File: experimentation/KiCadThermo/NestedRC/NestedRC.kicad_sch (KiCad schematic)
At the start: 12 parts

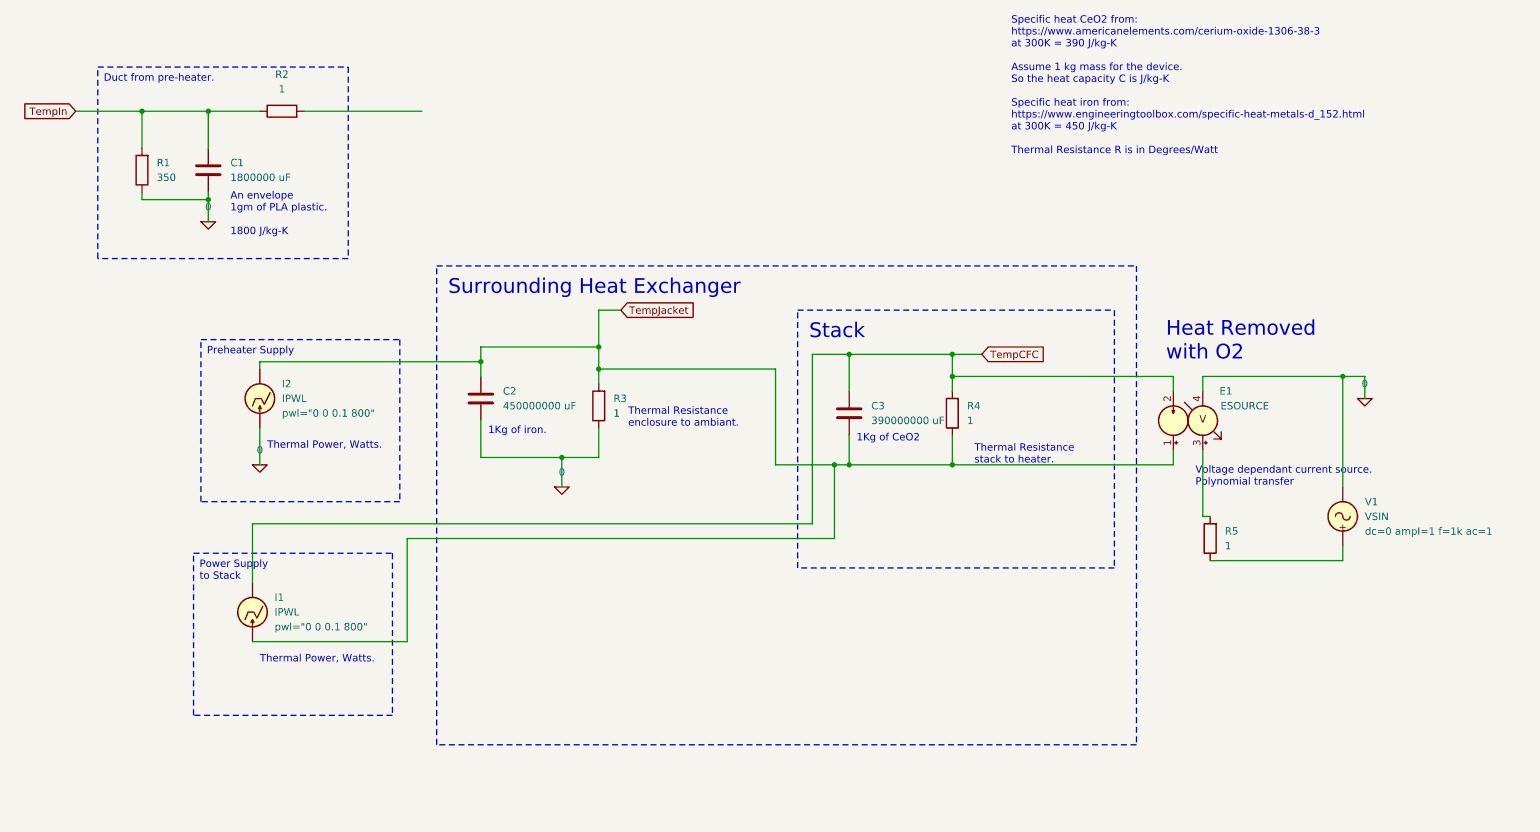
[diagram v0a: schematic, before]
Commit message: Add GPOLY to NestedRC circuit and set some values to make plots with which to experiment.
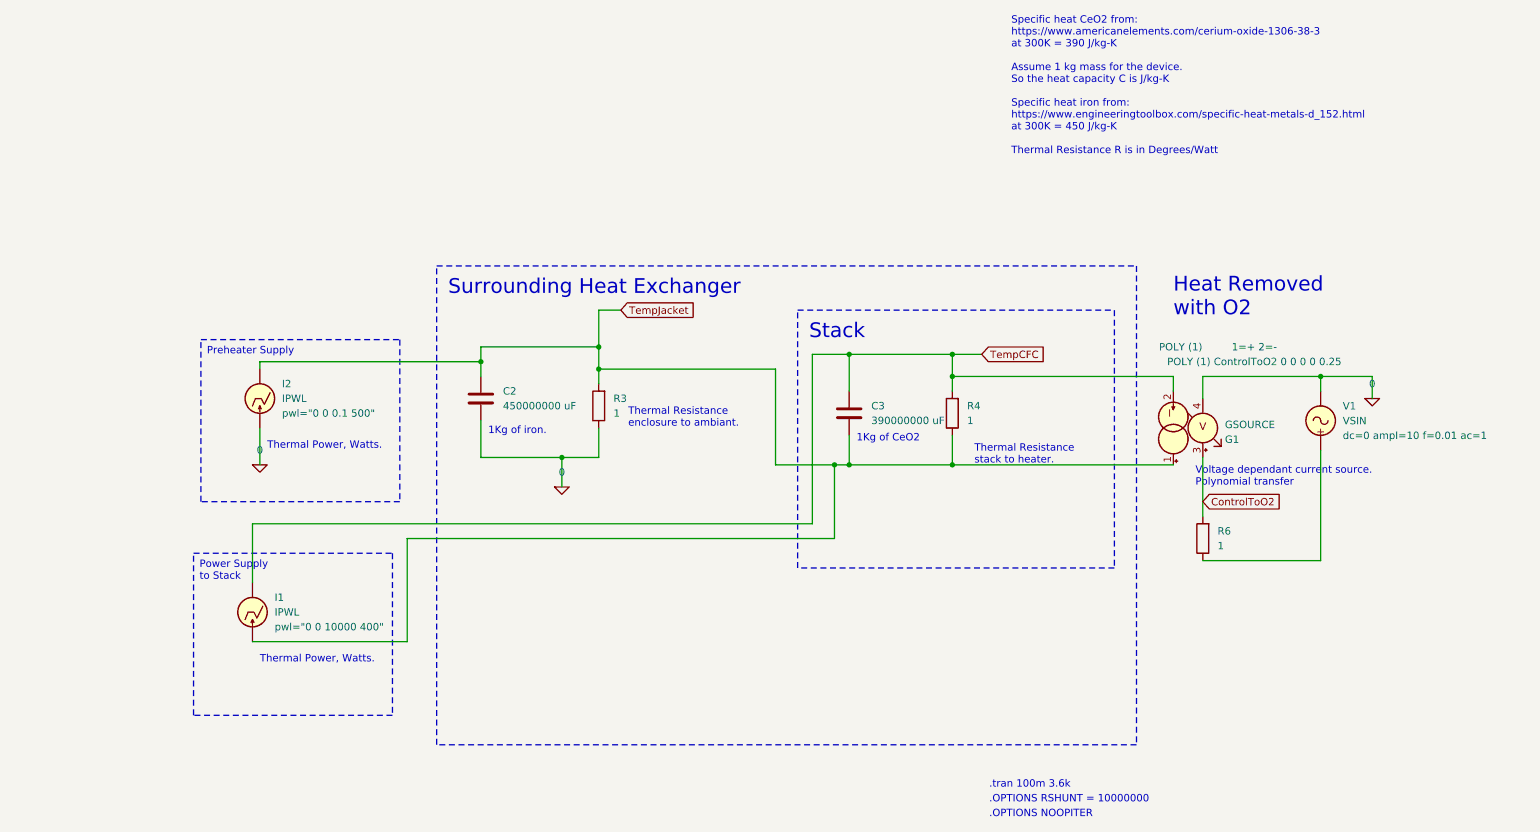
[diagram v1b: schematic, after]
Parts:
- removed C1: 1800000 uF, symbol Device:C
- removed E1: ESOURCE, symbol Simulation_SPICE:ESOURCE
- removed R1: 350, symbol Device:R
- removed R2: 1, symbol Device:R
- added G1: GSOURCE, symbol Simulation_SPICE:GSOURCE
- renumbered R5 to R6
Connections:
- net 0: now also G1.4 (C-)
- net TempCFC: now also G1.2 (N-)
- net TempJacket: now also G1.1 (N+)
- net ControlToO2: now reaches R6.2
- net ControlToO2: now also G1.3 (C+)
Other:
- note added: ".OPTIONS NOOPITER"
- note added: ".OPTIONS RSHUNT = 10000000"
- note added: ".tran 100m 3.6k"
- note removed: "An envelope 1gm of PLA plastic. 1800 J/kg-K"
- moved on the sheet: R6
